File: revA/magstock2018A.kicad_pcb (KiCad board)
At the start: 2 copper layers, 95.8 x 76.2 mm, 38 parts, among them J1 Audio In, J2 5vdcIn, J3 WS2813, J4 Conn_01x05, P1 USBMicroB-10118194-0001LF, P2 LOGO, SW1 TACTILE, SW2 TACTILE, SW3 TACTILE, SW4 TACTILE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

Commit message: Update to rev b.
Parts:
- added R7: 4k7, R_0805, F.Cu at (108.1, 82.1)
- added R8: 4k7, R_0805, F.Cu at (116.5, 89.8)
- added R9: 4k7, R_0805, F.Cu at (140.4, 79.6)
- J1: value Audio In -> Conn_01x03; footprint 35RAPC4BH3 -> 3.5mm_barrel_jack_MJ-3536N
- J4: footprint Molex_KK-6410-04_04x2.54mm_Straight -> Molex_KK-6410-05_05x2.54mm_Straight
- P2: value LOGO -> CONN_1
- R2, R3, R5: value 10k -> 4k7
- moved J1 13.3 mm to (108.6, 66.2), turned to 30 degrees
- moved C3 10.5 mm to (120.0, 70.0), turned to 0 degrees
- moved C2 6.15 mm to (114.6, 59.7), turned to 315 degrees
- moved C1 5.25 mm to (117.5, 62.4), turned to 0 degrees
- moved P1 1.21 mm to (171.4, 78.6)
- moved J4 0.51 mm to (135.1, 46.2)
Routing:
- net GND: track 333.8 -> 824.8 mm, vias 16 -> 21
- net +3V3: track 113.8 -> 138.9 mm, vias 6 -> 9
- net Net-(C2-Pad2): track 17.8 -> 7.09 mm, vias 1 -> 0
- net Net-(ESP1-Pad18): track 87.5 -> 97.8 mm
- net Net-(C3-Pad1): track 25.4 -> 15.5 mm
- net ANALOG: track 11.8 -> 19.8 mm
- net Net-(ESP1-Pad5): track 37.7 -> 42.9 mm
- net Net-(ESP1-Pad6): track 71.1 -> 75.8 mm
- net Net-(ESP1-Pad7): track 50.0 -> 53.0 mm
- net D-: track 87.7 -> 90.3 mm, vias 2 -> 4
- net D+: track 87.5 -> 89.7 mm, vias 2 -> 4
- net RXD: track 55.6 -> 57.3 mm
- net Net-(C1-Pad1): track 11.1 -> 12.5 mm, vias 2 -> 0
- net TUSB: track 16.3 -> 17.5 mm
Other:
- board text added: "0V"
- board text added: "0V BI DI 5V"
- board text added: "0V RX TX 5V G0"
- board text added: "5V"
- board text added: "M+ M-"
- board text added: "Rev B"

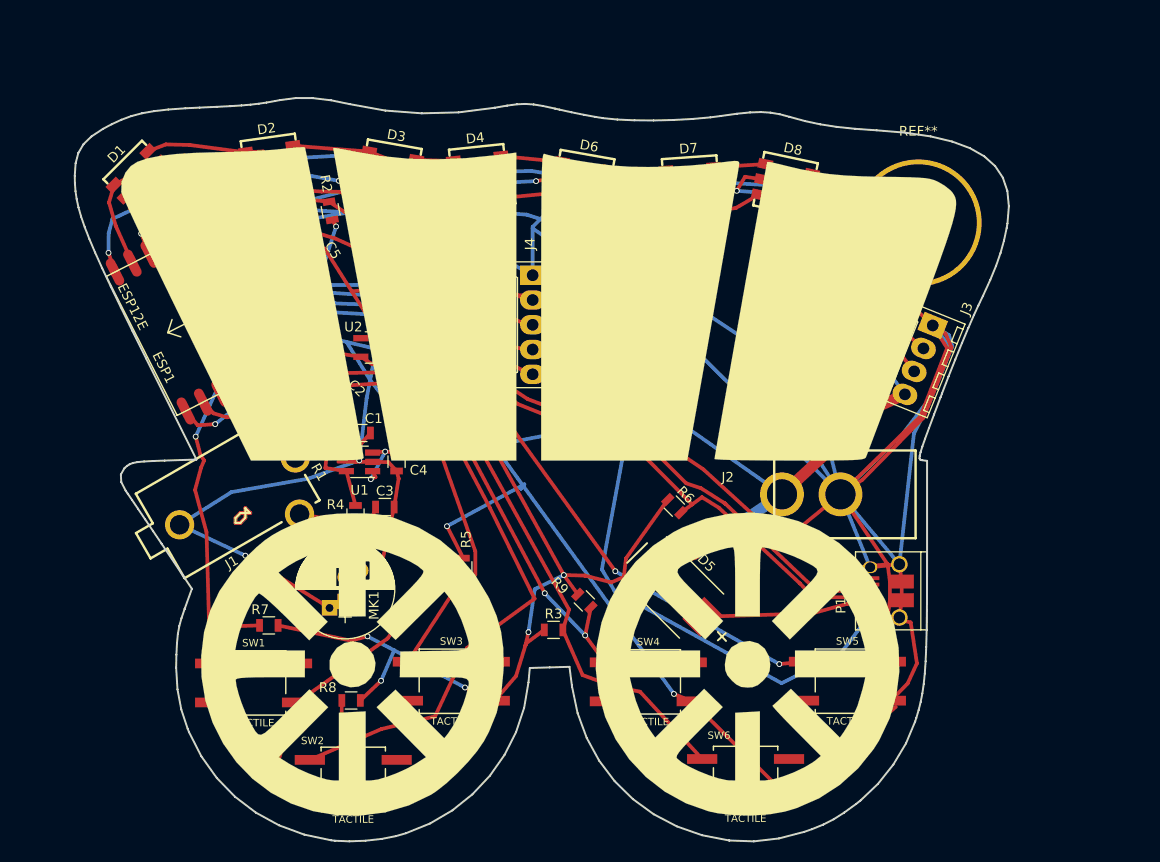
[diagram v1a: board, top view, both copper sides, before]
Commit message: Update to optional revc
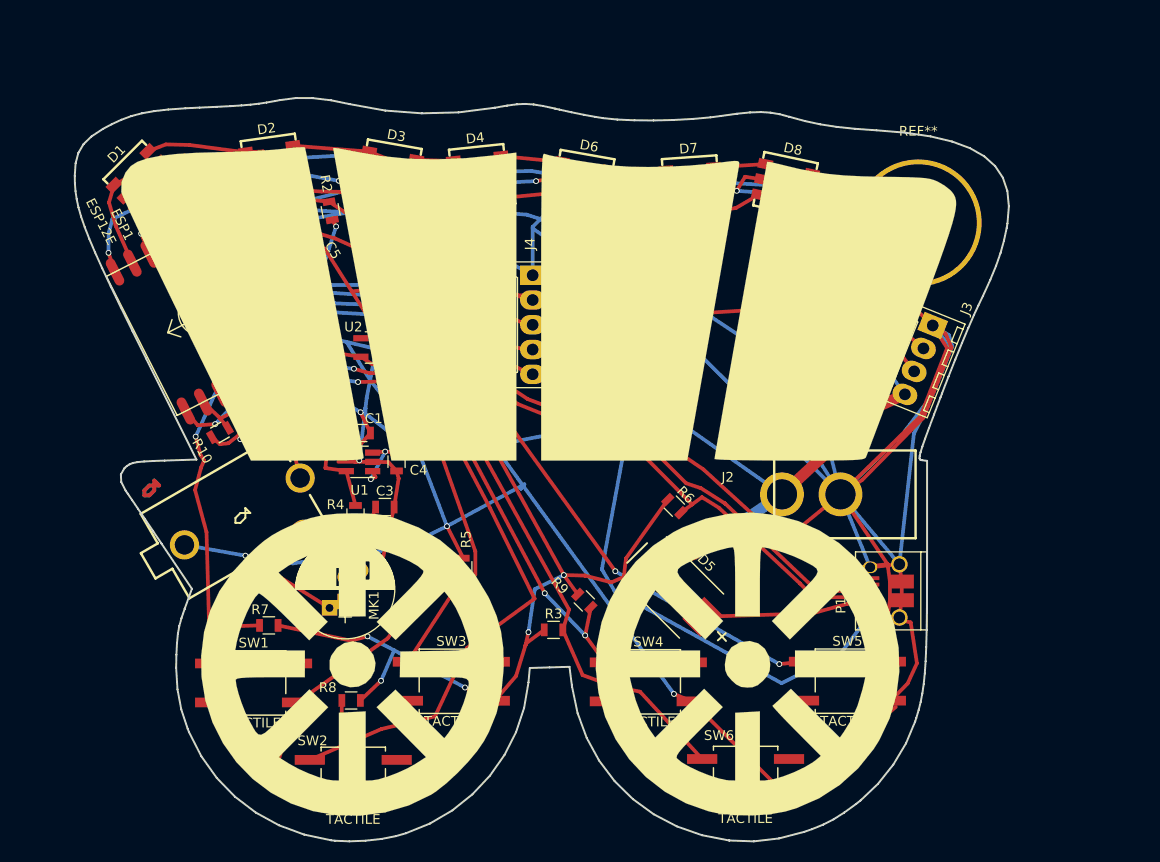
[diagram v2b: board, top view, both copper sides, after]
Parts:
- added R10: 47k, R_0805, F.Cu at (103.1, 62.4)
- added R11: 10k, R_0805, F.Cu at (108.9, 59.6)
- added R12: 4k7, R_0805, F.Cu at (105.8, 61.7)
- added R13: 47k, R_0805, F.Cu at (111.1, 61.0)
- added REF**: 1pin, Connect:1pin, F.Cu at (101.1, 50.1)
- added U3: OPAMP_MCP6001T, SOT-23-5, F.Cu at (111.3, 58.0)
- moved C2 7.21 mm to (107.5, 60.7), turned to 300 degrees
- moved R1 2.33 mm to (114.8, 60.2), turned to 165 degrees
- moved J1 2.12 mm to (109.1, 68.3)
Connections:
- net Net-(C1-Pad1) renamed AUDPWR
- ESP1 pad 2: ANALOG -> ADCPIN
- R1 pad 2: ANALOG -> VGS
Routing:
- net GND: track 824.8 -> 876.5 mm, vias 21 -> 23
- net Net-(R10-Pad1): track 0.00 -> 15.0 mm, vias 0 -> 2
- net ANALOG: track 19.8 -> 7.26 mm, vias 0 -> 2
- net ADCPIN: track 0.00 -> 11.4 mm
- net AUDPWR: track 12.5 -> 20.5 mm
- net VGS: track 0.00 -> 5.49 mm
- net Net-(ESP1-Pad5): track 42.9 -> 39.7 mm
- net Net-(ESP1-Pad1): track 10.5 -> 8.70 mm
- net +3V3: track 138.9 -> 137.2 mm
- net Net-(C2-Pad2): track 7.09 -> 6.55 mm
- net Net-(ESP1-Pad7): track 53.0 -> 52.4 mm
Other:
- board text added: "Rev C"
- board text removed: "Rev B"

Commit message: bump
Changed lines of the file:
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@@
-(kicad_pcb (version 4) (host pcbnew 4.0.2+dfsg1-stable)
+(kicad_pcb (version 4) (host pcbnew 4.0.7-e2-6376~58~ubuntu16.04.1)
   (general
     (links 119)
     (no_connects 0)
-    (area 41.805715 23.392 214.59 104.68565)
+    (area 41.955715 23.692 214.44 104.68565)
     (thickness 1.6)
     (drawings 29)
@@
     (35 F.Paste user)
     (36 B.SilkS user)
-    (37 F.SilkS user)
+    (37 F.SilkS user hide)
     (38 B.Mask user)
     (39 F.Mask user hide)
@@
     (tags "resistor 0805")
     (attr smd)
-    (fp_text reference C2 (at -2.032243 0.119948 390) (layer F.SilkS)
+    (fp_text reference C2 (at 5.256845 3.854878 570) (layer F.SilkS)
       (effects (font (size 1 1) (thickness 0.15)))
     )
@@
     (tags "resistor 0805")
     (attr smd)
-    (fp_text reference C6 (at 3.05 -0.43 90) (layer F.SilkS)
+    (fp_text reference C6 (at -0.09 -2.57 90) (layer F.SilkS)
       (effects (font (size 1 1) (thickness 0.15)))
     )
@@
     (tags "resistor 0805")
     (attr smd)
-    (fp_text reference R1 (at -0.186078 -1.544466 345) (layer F.SilkS)
+    (fp_text reference R1 (at -2.676394 1.679945 345) (layer F.SilkS)
       (effects (font (size 1 1) (thickness 0.15)))
     )
@@
     (tags "resistor 0805")
     (attr smd)
-    (fp_text reference R11 (at -2.920038 -1.062346 300) (layer F.SilkS)
+    (fp_text reference R11 (at -5.934139 -3.841769 300) (layer F.SilkS)
       (effects (font (size 1 1) (thickness 0.15)))
     )
@@
     (tags "resistor 0805")
     (attr smd)
-    (fp_text reference R12 (at 2.355448 -0.279756 390) (layer F.SilkS)
+    (fp_text reference R12 (at 1.727095 2.948583 390) (layer F.SilkS)
       (effects (font (size 1 1) (thickness 0.15)))
     )
@@
     (tags "resistor 0805")
     (attr smd)
-    (fp_text reference R13 (at 0.181821 -1.834923 210) (layer F.SilkS)
+    (fp_text reference R13 (at 0.153167 -5.985294 210) (layer F.SilkS)
       (effects (font (size 1 1) (thickness 0.15)))
     )
@@
     (tags SOT-23-5)
     (attr smd)
-    (fp_text reference U3 (at 2.962192 0.509334 30) (layer F.SilkS)
-      (effects (font (size 1 1) (thickness 0.15)))
-    )
+    (fp_text reference U3 (at 5.6873 2.729308 30) (layer F.SilkS)
+      (effects (font (size 1 1) (thickness 0.15)))
+    )

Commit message: Bump everything
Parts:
- added C7: 10u, R_0805, F.Cu at (118.3, 59.5)
- C3: value 2.2n10v -> NOPOP
- R10: value 47k -> 220k
- R12: value 4k7 -> 22k
- R7, R8, R9: value 4k7 -> NOPOP
- U1: value MCP1824 -> TLV70036
- moved J3 1.56 mm to (177.0, 50.1)
- moved J2 0.90 mm to (175.0, 69.3)
- moved P1 0.55 mm to (171.9, 78.6)
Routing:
- net VCC: track 223.1 -> 247.4 mm
- net GND: track 876.5 -> 889.2 mm, vias 23 -> 24
- net VGS: track 5.49 -> 10.3 mm, vias 0 -> 2
- net AUDPWR: track 20.5 -> 21.6 mm
- net Net-(D8-Pad3): track 24.8 -> 24.2 mm
- added copper zone on B.Cu, net GND
- added copper zone on F.Cu, net GND
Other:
- board text added: "Rev D"
- board text removed: "Rev C"

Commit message: push extra wire bridge
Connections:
- C4 pad 1: VCC -> TUSB
- C6 pad 1: VCC -> TUSB
- D1 pad 2: VCC -> TUSB
- D2 pad 2: VCC -> TUSB
- D3 pad 2: VCC -> TUSB
- D4 pad 2: VCC -> TUSB
- D5 pad 1: VCC -> TUSB
- D6 pad 2: VCC -> TUSB
- D7 pad 2: VCC -> TUSB
- D8 pad 2: VCC -> TUSB
- D9 pad 2: VCC -> TUSB
- J2 pad 2: VCC -> TUSB
- J3 pad 4: VCC -> TUSB
- J4 pad 4: VCC -> TUSB
- U1 pad 1: VCC -> TUSB
- U1 pad 3: VCC -> TUSB
- U2 pad 1: VCC -> TUSB
- U2 pad 3: VCC -> TUSB
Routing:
- net TUSB: track 17.5 -> 279.5 mm, vias 0 -> 15
- net VCC: track 247.4 -> 0.00 mm, vias 15 -> 0
